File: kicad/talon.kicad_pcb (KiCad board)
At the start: 2 copper layers, 157.7 x 112.7 mm, 38 parts, among them U1 nice_nano

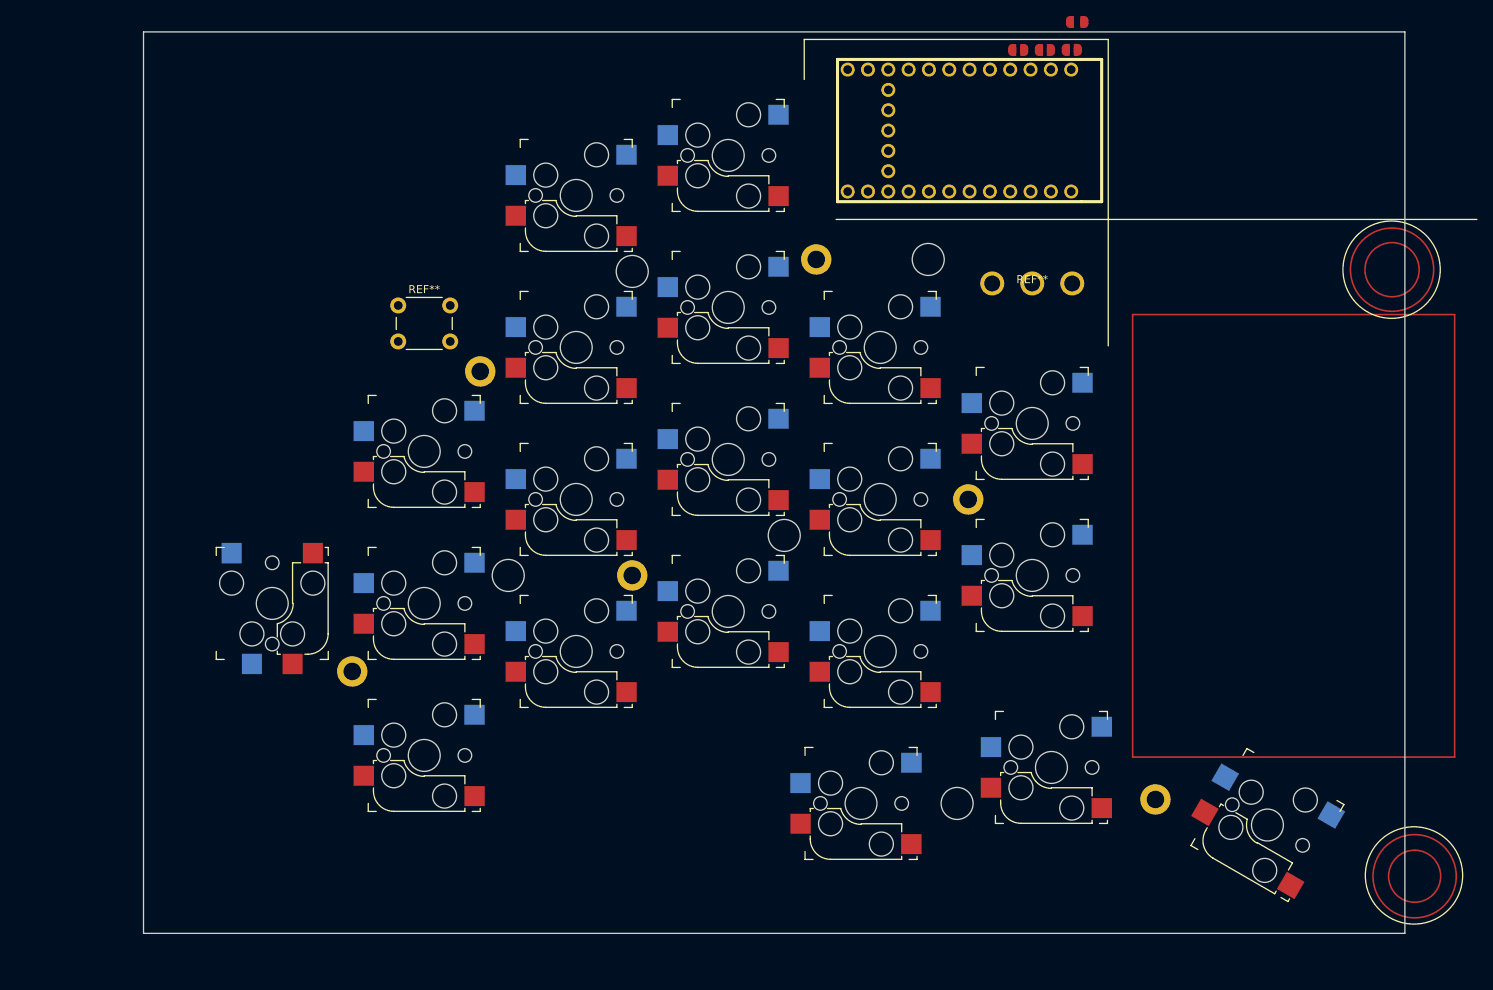
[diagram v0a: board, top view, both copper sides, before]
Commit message: added fillet to pcb
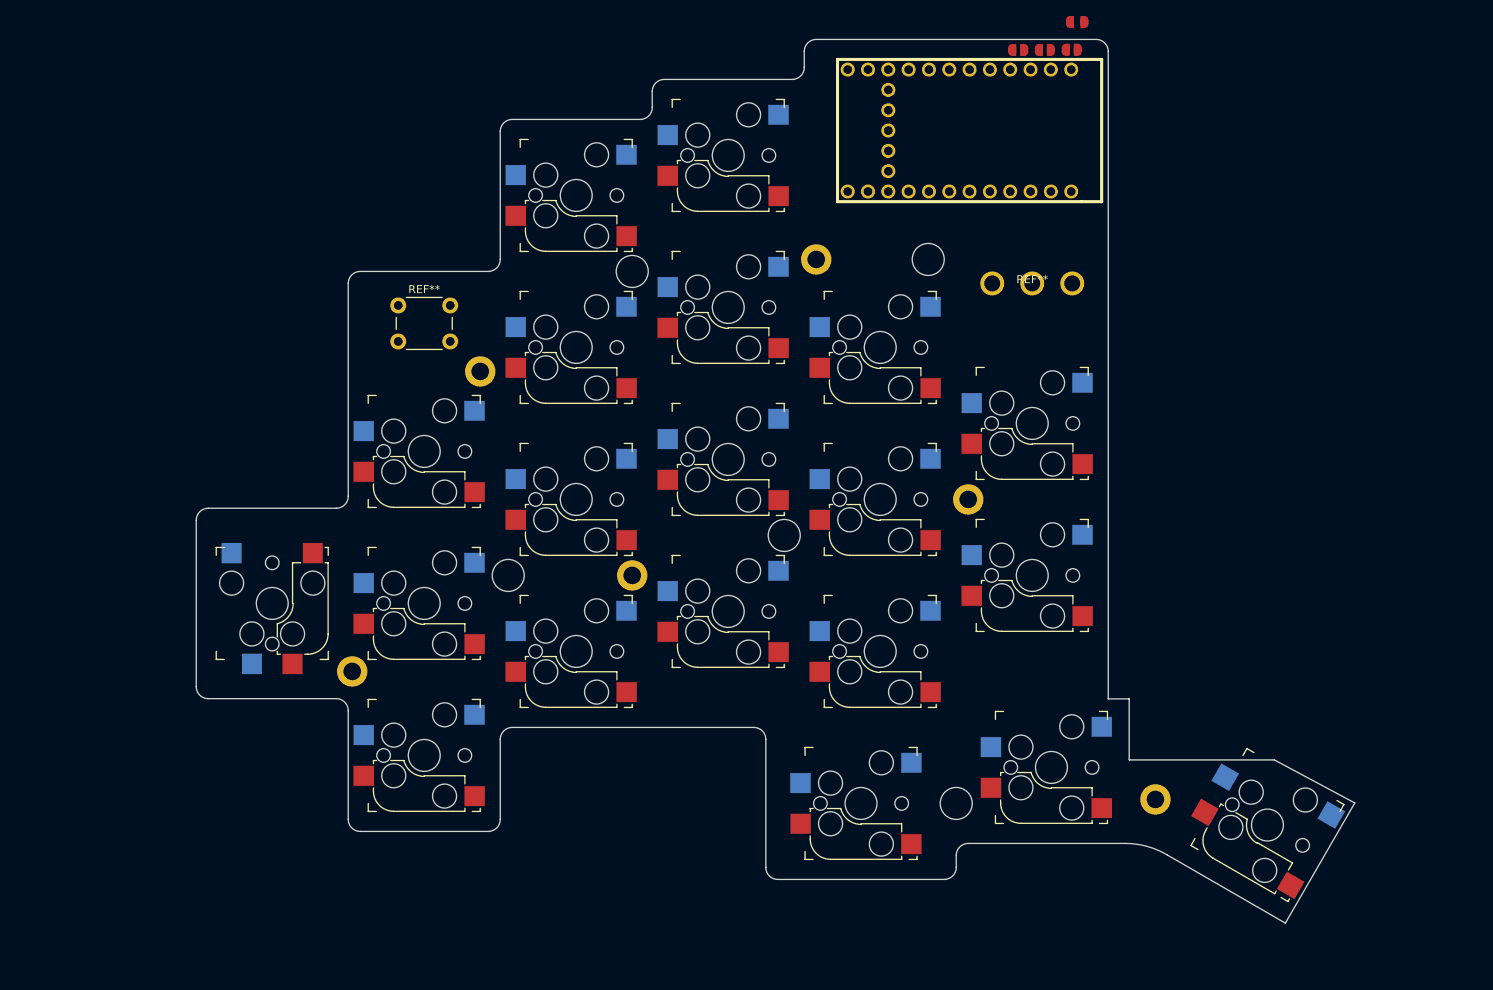
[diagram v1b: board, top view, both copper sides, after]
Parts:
- moved REF** 0.11 mm to (178.5, 142.0)
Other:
- board size 157.7 x 112.7 mm -> 144.8 x 110.5 mm

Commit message: working on routing
Battery connection gnd is disconnected from fill.
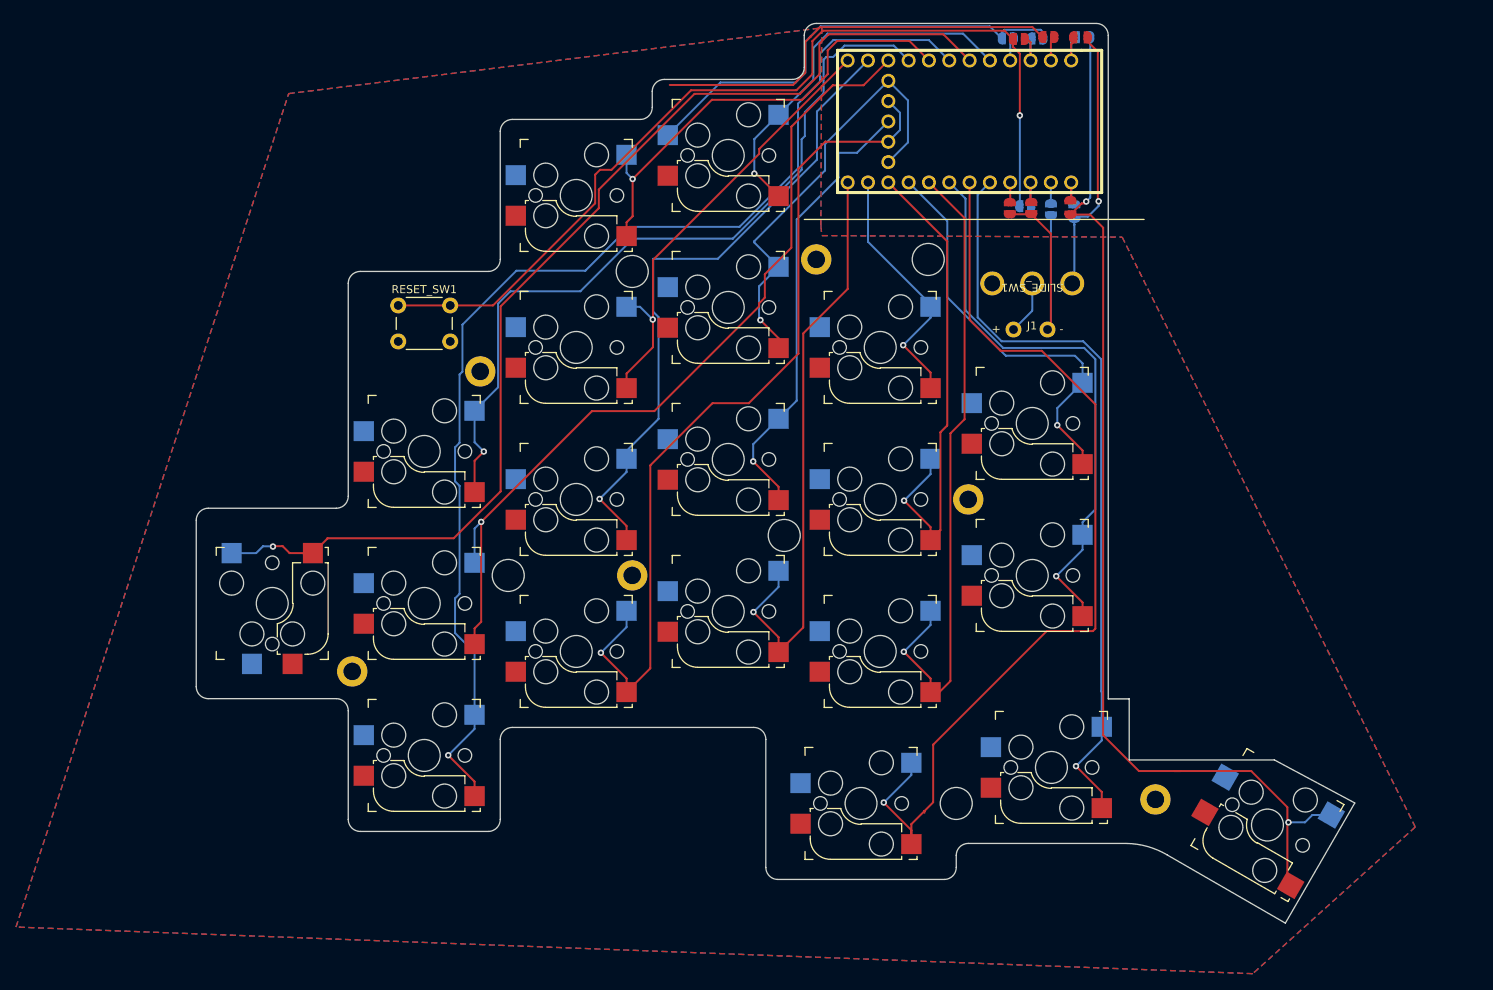
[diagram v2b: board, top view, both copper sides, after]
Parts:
- removed the REF** at (193.9, 44.4)
- removed the REF** at (186.2, 47.8)
- removed the REF** at (192.9, 47.8)
- removed the REF** at (189.6, 47.8)
- added J1: JST connector, footprints:power_connector, F.Cu at (188.0, 82.8)
- added JP1: Jumper_2_Open, footprints:Jumper_Open_0.8mm, F.Cu at (193.7, 46.2)
- added JP11: Jumper_2_Open, footprints:Jumper_Open_0.5mm, B.Cu at (190.3, 67.8)
- added JP12: Jumper_2_Open, footprints:Jumper_Open_0.5mm, B.Cu at (187.1, 67.3)
- added JP13: Jumper_2_Open, footprints:Jumper_Open_0.5mm, F.Cu at (187.9, 67.6)
- added JP14: Jumper_2_Open, footprints:Jumper_Open_0.5mm, F.Cu at (185.2, 67.6)
- added JP2: Jumper_2_Open, footprints:Jumper_Open_0.8mm, B.Cu at (194.1, 46.3)
- added JP4: Jumper_2_Open, footprints:Jumper_Open_0.5mm, F.Cu at (190.0, 46.2)
- added JP5: Jumper_2_Open, footprints:Jumper_Open_0.5mm, F.Cu at (186.3, 46.4)
- added JP6: Jumper_2_Open, footprints:Jumper_Open_0.5mm, B.Cu at (188.6, 46.4)
- added JP7: Jumper_2_Open, footprints:Jumper_Open_0.5mm, B.Cu at (184.9, 46.4)
- added JP8: Jumper_2_Open, footprints:Jumper_Open_0.8mm, B.Cu at (193.2, 67.7)
- added JP9: Jumper_2_Open, footprints:Jumper_Open_0.8mm, F.Cu at (192.8, 67.2)
- RESET_SW1: renamed from REF**; value SW_PUSH_6mm -> SW_Push
- SLIDE_SW1: renamed from REF**; value slide_switch_5mm -> SW_SPDT
- SW1, SW10, SW13, SW15, SW16, SW18, SW19, SW2, SW20, SW4, SW5, SW6, SW7, SW8, SW9: renamed from REF**; value Kailh_socket_MX_reversible -> SW_Push
- locked (x3): value Kailh_socket_MX_reversible -> SW_Push
- moved U1 1.14 mm to (178.9, 56.8)
- turned SLIDE_SW1 to 180 degrees
- renumbered REF** to SW11, REF** to SW3
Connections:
- RESET_SW1 pad 1: (no net) -> RESET
- RESET_SW1 pad 2: (no net) -> GND
- SLIDE_SW1 pad 1: (no net) -> BATIN
- SLIDE_SW1 pad 2: (no net) -> Net-(J1-Pin_1)
- SLIDE_SW1 pad 3: (no net) -> unconnected-(SLIDE_SW1-C-Pad3)
- SW1 pad 1: (no net) -> P8
- SW1 pad 2: (no net) -> GND
- SW10 pad 1: (no net) -> P11
- SW10 pad 2: (no net) -> GND
- SW11 pad 1: (no net) -> P33
- SW11 pad 2: (no net) -> GND
- SW13 pad 1: (no net) -> P18
- SW13 pad 2: (no net) -> GND
- SW15 pad 1: (no net) -> P32
- SW15 pad 2: (no net) -> GND
- SW16 pad 1: (no net) -> P13
- SW16 pad 2: (no net) -> GND
- SW18 pad 1: (no net) -> P19
- SW18 pad 2: (no net) -> GND
- SW19 pad 1: (no net) -> P20
- SW19 pad 2: (no net) -> GND
- SW2 pad 1: (no net) -> P5
- SW2 pad 2: (no net) -> GND
- SW20 pad 1: (no net) -> P1
- SW20 pad 2: (no net) -> GND
- SW3 pad 1: (no net) -> P9
- SW3 pad 2: (no net) -> GND
- SW4 pad 1: (no net) -> P12
- SW4 pad 2: (no net) -> GND
- SW5 pad 1: (no net) -> P31
- SW5 pad 2: (no net) -> GND
- SW6 pad 1: (no net) -> P14
- SW6 pad 2: (no net) -> GND
- SW7 pad 1: (no net) -> P16
- SW7 pad 2: (no net) -> GND
- SW8 pad 1: (no net) -> P6
- SW8 pad 2: (no net) -> GND
- SW9 pad 1: (no net) -> P10
- SW9 pad 2: (no net) -> GND
- U1 pad 1: (no net) -> Net-(JP1-B)
- U1 pad 10: (no net) -> P10
- U1 pad 11: (no net) -> P11
- U1 pad 12: (no net) -> P12
- U1 pad 13: (no net) -> P13
- U1 pad 14: (no net) -> P14
- U1 pad 15: (no net) -> P15
- U1 pad 16: (no net) -> P16
- U1 pad 17: (no net) -> P17
- U1 pad 18: (no net) -> P18
- U1 pad 19: (no net) -> P19
- U1 pad 2: (no net) -> Net-(JP4-B)
- U1 pad 20: (no net) -> P20
- U1 pad 21: (no net) -> Net-(JP14-B)
- U1 pad 22: (no net) -> Net-(JP12-B)
- U1 pad 23: (no net) -> Net-(JP11-B)
- U1 pad 24: (no net) -> Net-(JP8-B)
- U1 pad 3: (no net) -> Net-(JP5-B)
- U1 pad 31: (no net) -> P31
- U1 pad 32: (no net) -> P32
- U1 pad 33: (no net) -> P33
- U1 pad 4: (no net) -> Net-(JP7-B)
- U1 pad 5: (no net) -> P5
- U1 pad 6: (no net) -> P6
- U1 pad 7: (no net) -> P7
- U1 pad 8: (no net) -> P8
- U1 pad 9: (no net) -> P9
- locked pad 1: (no net) -> P17
- locked pad 2: (no net) -> GND (x3)
- locked pad 1: (no net) -> P15
- locked pad 1: (no net) -> P7
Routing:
- net P7: track 0.00 -> 147.0 mm, vias 0 -> 1
- net GND: track 0.00 -> 142.5 mm
- net P6: track 0.00 -> 138.4 mm, vias 0 -> 1
- net P1: track 0.00 -> 134.9 mm, vias 0 -> 2
- net P19: track 0.00 -> 118.4 mm, vias 0 -> 1
- net RESET: track 0.00 -> 117.3 mm, vias 0 -> 1
- net P32: track 0.00 -> 108.7 mm, vias 0 -> 1
- net P10: track 0.00 -> 106.6 mm, vias 0 -> 1
- net P9: track 0.00 -> 97.6 mm, vias 0 -> 1
- net P20: track 0.00 -> 93.9 mm, vias 0 -> 1
- net P17: track 0.00 -> 80.9 mm, vias 0 -> 1
- net P11: track 0.00 -> 80.5 mm, vias 0 -> 1
- net P13: track 0.00 -> 75.1 mm, vias 0 -> 1
- net P18: track 0.00 -> 71.1 mm, vias 0 -> 1
- net P15: track 0.00 -> 61.5 mm, vias 0 -> 1
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- added copper zone on B.Cu, net GND
- added copper zone on F.Cu, net GND
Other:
- board size 144.8 x 110.5 mm -> 144.8 x 112.5 mm

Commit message: PCB seems legit
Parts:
- renumbered REF** to HOLE1, REF** to HOLE2, REF** to HOLE3, REF** to HOLE4, REF** to MOUNT1, REF** to MOUNT2, REF** to MOUNT3, REF** to MOUNT4, REF** to MOUNT5, REF** to MOUNT6
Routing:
- net GND: track 142.5 -> 75.0 mm, vias 0 -> 2
- net P6: track 138.4 -> 130.8 mm
- net P19: track 118.4 -> 111.8 mm
- net P7: track 147.0 -> 150.0 mm
- net P10: track 106.6 -> 103.9 mm
- net P31: track 55.8 -> 53.3 mm
- net RESET: track 117.3 -> 115.4 mm
- net P12: track 56.3 -> 58.0 mm
- net P8: track 57.7 -> 59.3 mm
- net P9: track 97.6 -> 98.7 mm
- net P18: track 71.1 -> 72.0 mm
- net P33: track 57.0 -> 56.1 mm
- net P16: track 51.9 -> 52.5 mm
- net P11: track 80.5 -> 81.1 mm
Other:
- board size 144.8 x 112.5 mm -> 145 x 112.5 mm

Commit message: v1 sent for production
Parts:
- moved MOUNT2 9.06 mm to (112.0, 126.5)
